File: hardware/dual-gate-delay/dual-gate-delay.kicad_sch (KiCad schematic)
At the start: 55 parts, among them J1 MonoJack, J2 MonoJack, J3 MonoJack, J4 Conn_02x03_Odd_Even, J5 MonoJack, J6 MonoJack, J7 MonoJack, J8 Conn_02x03_Odd_Even, J9 Conn_02x05_Odd_Even, Q1 BC547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

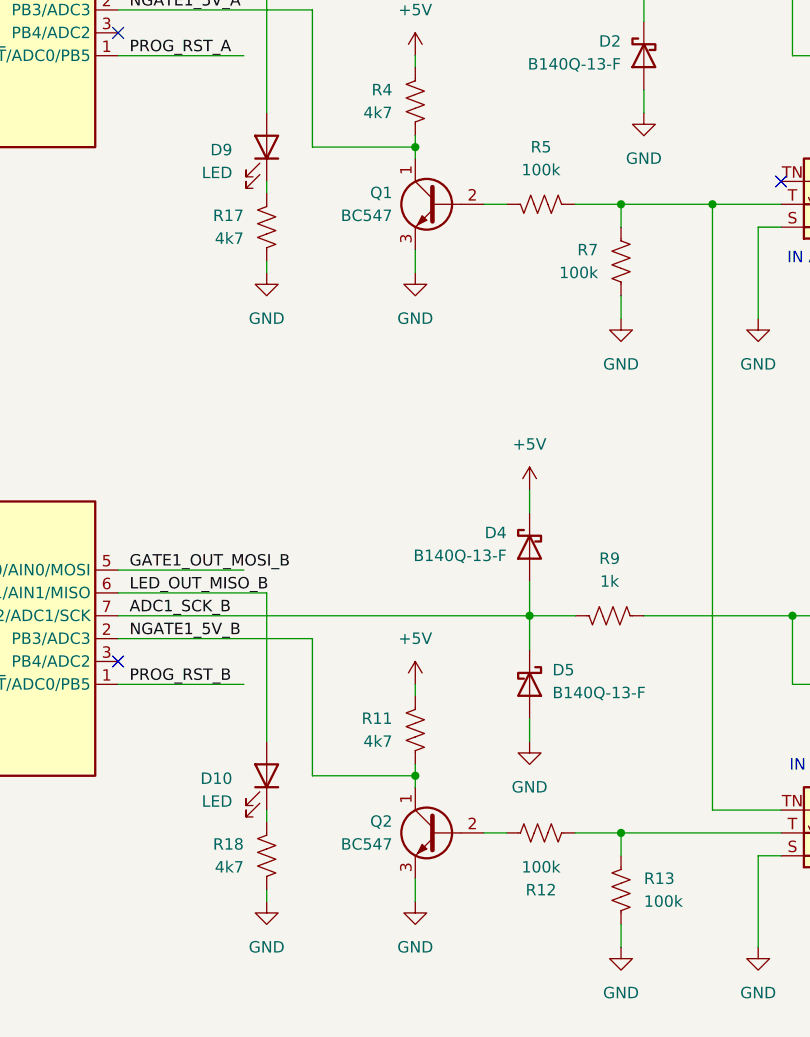
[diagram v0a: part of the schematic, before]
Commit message: Initial project for dual gate delay faceplate, small PBC revisions (SMT BJTs, moved LED)
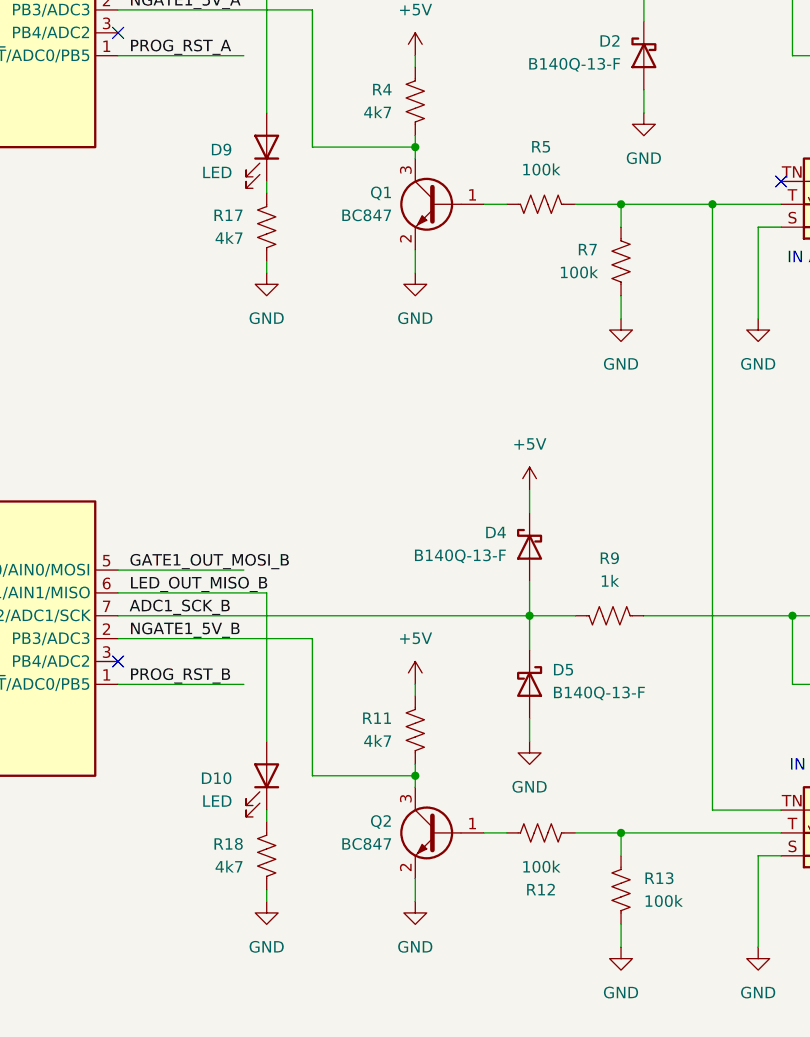
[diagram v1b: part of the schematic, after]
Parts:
- removed Q1, Q2: BC547, Package_TO_SOT_THT:TO-92_Inline_Wide, symbol Transistor_BJT:BC547
- added Q1, Q2: BC847, Package_TO_SOT_SMD:SOT-23, symbol Transistor_BJT:BC847
- R15, R16: footprint Resistor_THT:R_Axial_DIN0207_L6.3mm_D2.5mm_P10.16mm_Horizontal -> Resistor_SMD:R_0805_2012Metric_Pad1.20x1.40mm_HandSolder
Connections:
- net GND: now also Q1.2 (E), Q2.2 (E)
- net NGATE1_5V_A: now also Q1.3 (C)
- net NGATE1_5V_B: now also Q2.3 (C)
- net at R12.2: now also Q2.1 (B)
- net at R5.2: now also Q1.1 (B)
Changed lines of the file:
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@@
 	(title_block
 		(title "Dual Gate Delay")
-		(date "2025-09-17")
-		(rev "1.0")
+		(date "2025-10-18")
+		(rev "1.1")
 		(company "idyllm")
 		(comment 1 "CC BY-SA 4.0")
@@
 	)
 	(symbol
+		(lib_id "Transistor_BJT:BC847")
+		(at 101.6 134.62 0)
+		(mirror y)
+		(unit 1)
+		(exclude_from_sim no)
+		(in_bom yes)
+		(on_board yes)
+		(dnp no)
+		(fields_autoplaced yes)
+		(property "Reference" "Q2"
+			(at 96.52 133.3499 0)
+			(effects
+				(font
+					(size 1.27 1.27)
+				)
+				(justify left)
+			)
+		)
+		(property "Value" "BC847"
+			(at 96.52 135.8899 0)
+			(effects
+				(font
+					(size 1.27 1.27)
+				)
+				(justify left)
+			)
+		)
+		(property "Footprint" "Package_TO_SOT_SMD:SOT-23"
+			(at 96.52 136.525 0)
+			(effects
+				(font
+					(size 1.27 1.27)
+					(italic yes)
+				)
+				(justify left)
+				(hide yes)
+			)
+		)
+		(property "Datasheet" "http://www.infineon.com/dgdl/Infineon-BC847SERIES_BC848SERIES_BC849SERIES_BC850SERIES-DS-v01_01-en.pdf?fileId=db3a304314dca389011541d4630a1657"
+			(at 101.6 134.62 0)
+			(effects
+				(font
+					(size 1.27 1.27)
+				)
+				(justify left)
+				(hide yes)
+			)
+		)
+		(property "Description" "0.1A Ic, 45V Vce, NPN Transistor, SOT-23"
+			(at 101.6 134.62 0)
+			(effects
+				(font
+					(size 1.27 1.27)
+				)
+				(hide yes)
+			)
+		)
+		(pin "2"
+		)
+		(pin "1"
+		)
+		(pin "3"
+		)
+		(instances
+			(project ""
+				(path "/37f03a04-246d-4755-9a59-ecba12d4b238"
+					(reference "Q2")
+					(unit 1)
+				)
+			)
+		)
+	)
+	(symbol
 		(lib_id "Device:R_US")
 		(at 113.03 134.62 270)
@@
 			)
 		)
-		(property "Footprint" "Resistor_THT:R_Axial_DIN0207_L6.3mm_D2.5mm_P10.16mm_Horizontal"
+		(property "Footprint" "Resistor_SMD:R_0805_2012Metric_Pad1.20x1.40mm_HandSolder"
 			(at 89.154 171.704 90)
 			(effects
@@
 			)
 		)
-		(property "Footprint" "Resistor_THT:R_Axial_DIN0207_L6.3mm_D2.5mm_P10.16mm_Horizontal"
+		(property "Footprint" "Resistor_SMD:R_0805_2012Metric_Pad1.20x1.40mm_HandSolder"
 			(at 89.154 181.864 90)
 			(effects
@@
 	)
 	(symbol
-		(lib_id "Transistor_BJT:BC547")
-		(at 101.6 64.77 0)
-		(mirror y)
-		(unit 1)
-		(exclude_from_sim no)
-		(in_bom yes)
-		(on_board yes)
-		(dnp no)
-		(fields_autoplaced yes)
-		(property "Reference" "Q1"
-			(at 96.52 63.4999 0)
-			(effects
-				(font
-					(size 1.27 1.27)
-				)
-				(justify left)
-			)
-		)
-		(property "Value" "BC547"
-			(at 96.52 66.0399 0)
-			(effects
-				(font
-					(size 1.27 1.27)
-				)
-				(justify left)
-			)
-		)
-		(property "Footprint" "Package_TO_SOT_THT:TO-92_Inline_Wide"
-			(at 96.52 66.675 0)
-			(effects
-				(font
-					(size 1.27 1.27)
-					(italic yes)
-				)
-				(justify left)
-				(hide yes)
-			)
-		)
-		(property "Datasheet" "https://www.onsemi.com/pub/Collateral/BC550-D.pdf"
-			(at 101.6 64.77 0)
-			(effects
-				(font
-					(size 1.27 1.27)
-				)
-				(justify left)
-				(hide yes)
-			)
-		)
-		(property "Description" "0.1A Ic, 45V Vce, Small Signal NPN Transistor, TO-92"
-			(at 101.6 64.77 0)
-			(effects
-				(font
-					(size 1.27 1.27)
-				)
-				(hide yes)
-			)
-		)
-		(pin "3"
-		)
-		(pin "1"
-		)
-		(pin "2"
-		)
-		(instances
-			(project "dual-gate-delay"
-				(path "/37f03a04-246d-4755-9a59-ecba12d4b238"
-					(reference "Q1")
-					(unit 1)
-				)
-			)
-		)
-	)
-	(symbol
 		(lib_id "Amplifier_Operational:TL074")
 		(at 232.41 46.99 0)
@@
 	)
 	(symbol
+		(lib_id "Transistor_BJT:BC847")
+		(at 101.6 64.77 0)
+		(mirror y)
+		(unit 1)
+		(exclude_from_sim no)
+		(in_bom yes)
+		(on_board yes)
+		(dnp no)
+		(fields_autoplaced yes)
+		(property "Reference" "Q1"
+			(at 96.52 63.4999 0)
+			(effects
+				(font
+					(size 1.27 1.27)
+				)
+				(justify left)
+			)
+		)
+		(property "Value" "BC847"
+			(at 96.52 66.0399 0)
+			(effects
+				(font
+					(size 1.27 1.27)
+				)
+				(justify left)
+			)
+		)
+		(property "Footprint" "Package_TO_SOT_SMD:SOT-23"
+			(at 96.52 66.675 0)
+			(effects
+				(font
+					(size 1.27 1.27)
+					(italic yes)
+				)
+				(justify left)
+				(hide yes)
+			)
+		)
+		(property "Datasheet" "http://www.infineon.com/dgdl/Infineon-BC847SERIES_BC848SERIES_BC849SERIES_BC850SERIES-DS-v01_01-en.pdf?fileId=db3a304314dca389011541d4630a1657"
+			(at 101.6 64.77 0)
+			(effects
+				(font
+					(size 1.27 1.27)
+				)
+				(justify left)
+				(hide yes)
+			)
+		)
+		(property "Description" "0.1A Ic, 45V Vce, NPN Transistor, SOT-23"
+			(at 101.6 64.77 0)
+			(effects
+				(font
+					(size 1.27 1.27)
+				)
+				(hide yes)
+			)
+		)
+		(pin "2"
+		)
+		(pin "1"
+		)
+		(pin "3"
+		)
+		(instances
+			(project ""
+				(path "/37f03a04-246d-4755-9a59-ecba12d4b238"
+					(reference "Q1")
+					(unit 1)
+				)
+			)
+		)
+	)
+	(symbol
 		(lib_id "Connector_Audio:AudioJack2_SwitchT")
 		(at 144.78 134.62 180)
@@
 					(unit 1)
 				)
-			)
-		)
-	)
-	(symbol
-		(lib_id "Transistor_BJT:BC547")
-		(at 101.6 134.62 0)
-		(mirror y)
-		(unit 1)
-		(exclude_from_sim no)
-		(in_bom yes)
-		(on_board yes)
-		(dnp no)
-		(fields_autoplaced yes)
-		(property "Reference" "Q2"
-			(at 96.52 133.3499 0)
-			(effects
-				(font
-					(size 1.27 1.27)
-				)
-				(justify left)
-			)
-		)
-		(property "Value" "BC547"
-			(at 96.52 135.8899 0)
-			(effects
-				(font
-					(size 1.27 1.27)
-				)
-				(justify left)
-			)
-		)
-		(property "Footprint" "Package_TO_SOT_THT:TO-92_Inline_Wide"
-			(at 96.52 136.525 0)
-			(effects
-				(font
-					(size 1.27 1.27)
-					(italic yes)
-				)
-				(justify left)
-				(hide yes)
-			)
-		)
-		(property "Datasheet" "https://www.onsemi.com/pub/Collateral/BC550-D.pdf"
-			(at 101.6 134.62 0)
-			(effects
-				(font
-					(size 1.27 1.27)
-				)
-				(justify left)
-				(hide yes)
-			)
-		)
-		(property "Description" "0.1A Ic, 45V Vce, Small Signal NPN Transistor, TO-92"
-			(at 101.6 134.62 0)
-			(effects
-				(font
-					(size 1.27 1.27)
-				)
-				(hide yes)
-			)
-		)
-		(pin "3"
-		)
-		(pin "1"
-		)
-		(pin "2"
-		)
-		(instances
-			(project "dual-gate-delay"
-				(path "/37f03a04-246d-4755-9a59-ecba12d4b238"
-					(reference "Q2")
-					(unit 1)
-				)
